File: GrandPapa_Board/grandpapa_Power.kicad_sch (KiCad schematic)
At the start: 33 parts, among them U1 LT1576IS8-5#TRPBF, U2 TPS61023DRLT, U5 FPF2124, U6 INA180

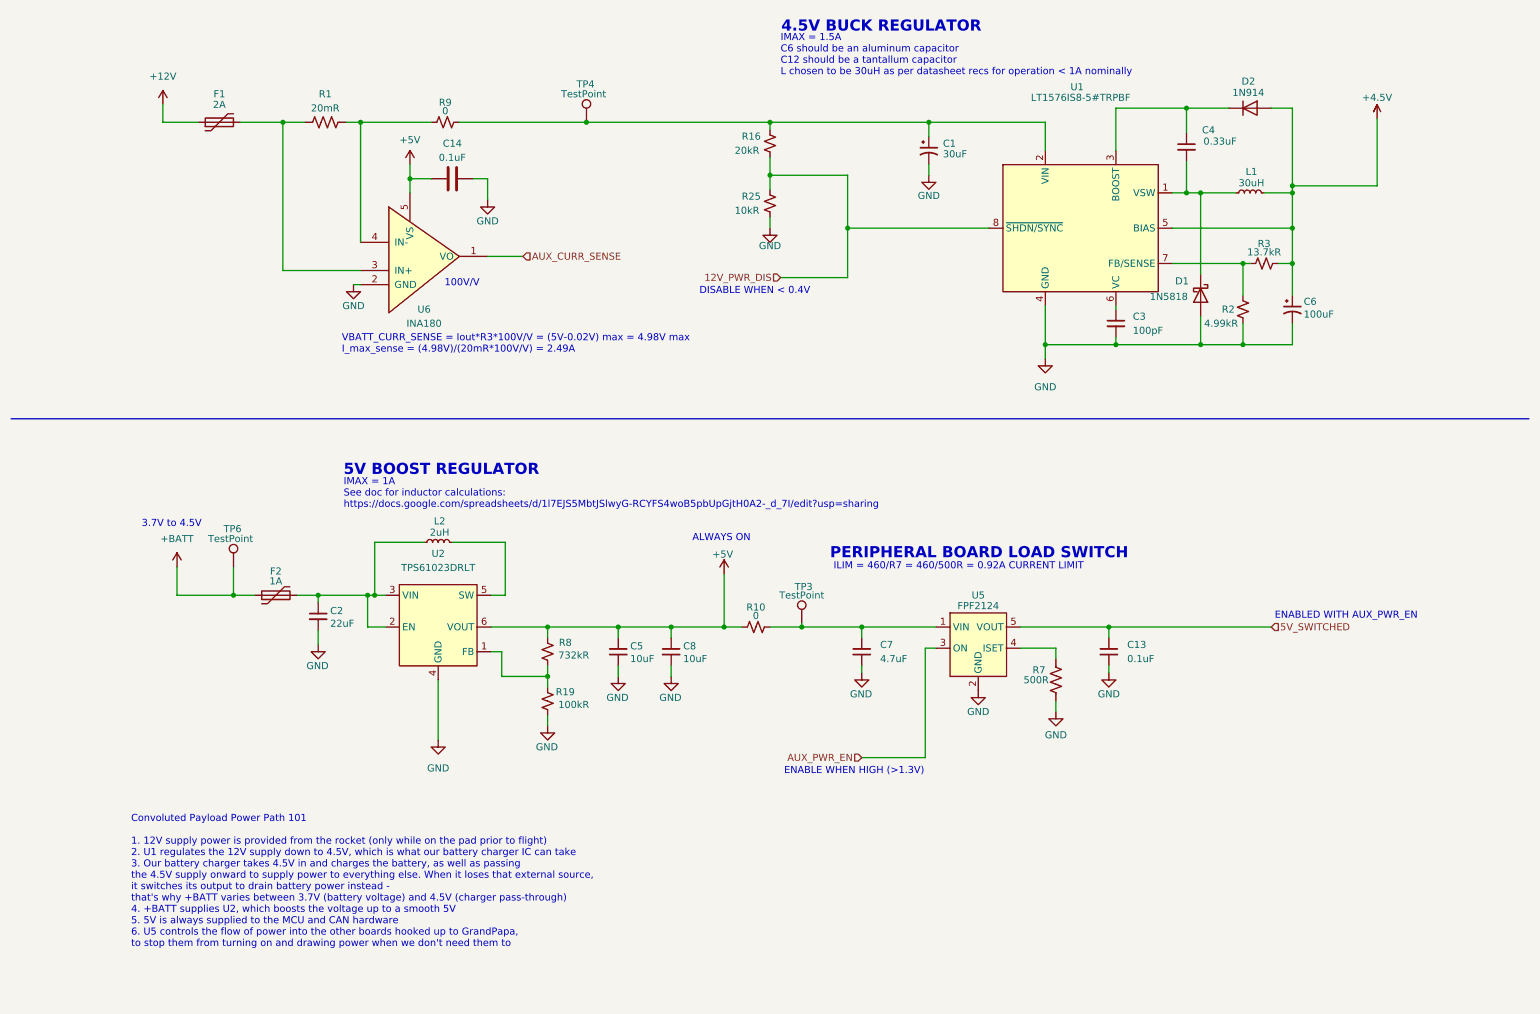
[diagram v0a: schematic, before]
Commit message: added new buck reg IC, external component values TBA
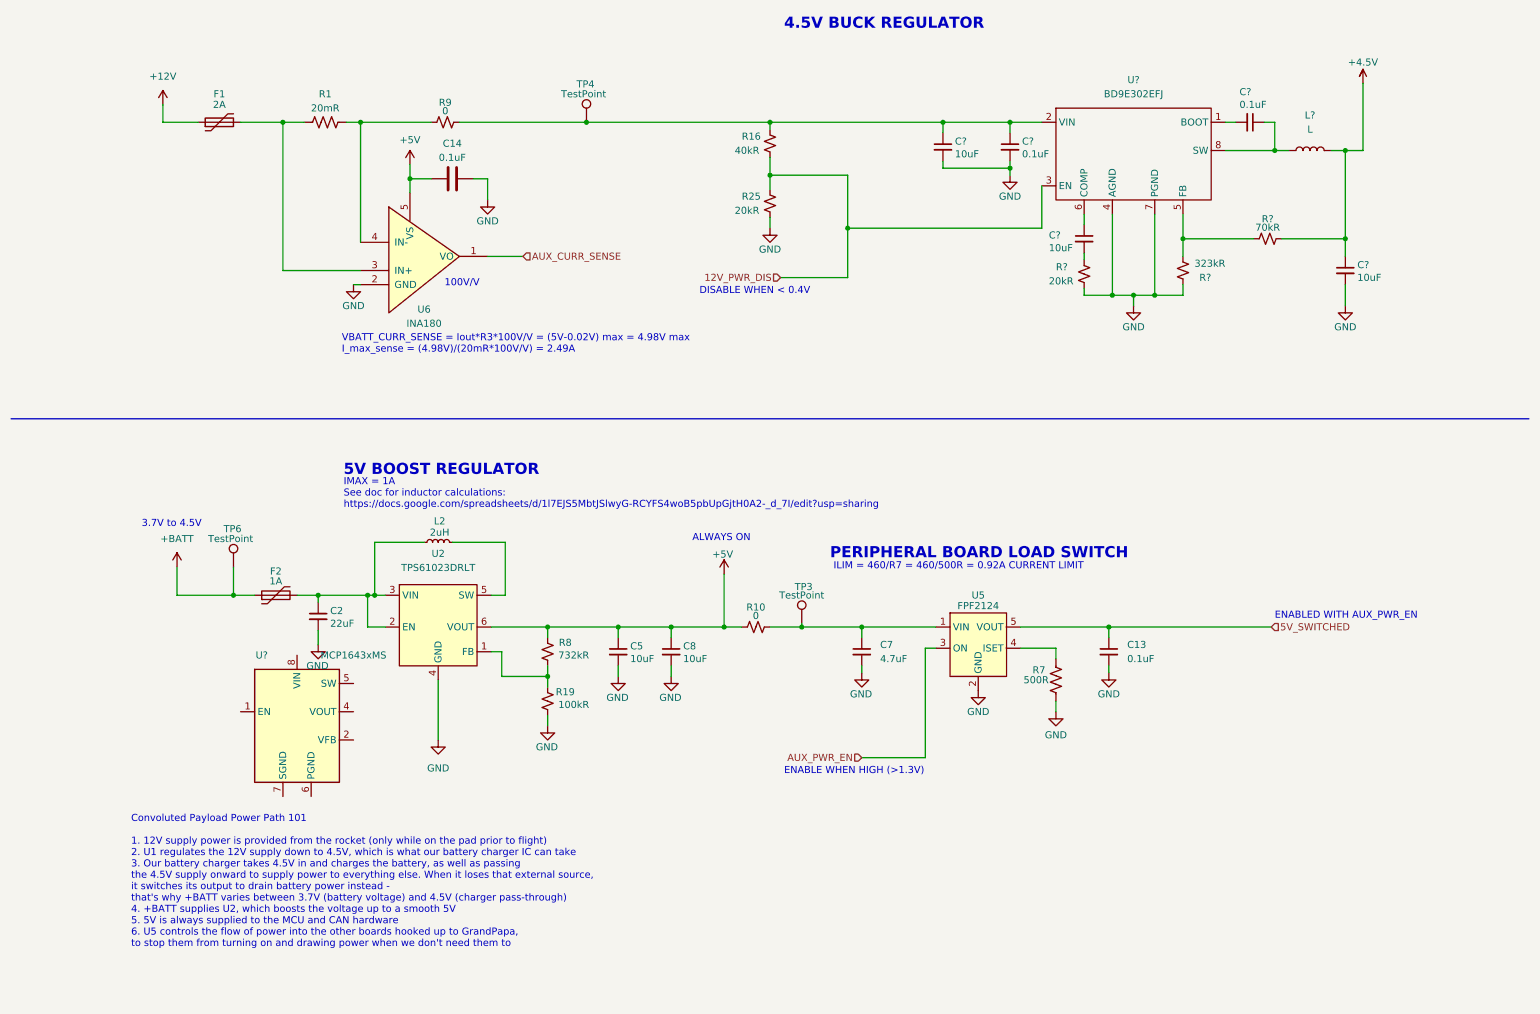
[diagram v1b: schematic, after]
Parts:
- removed C1: 30uF, symbol Device:C_Polarized_Small_US
- removed C3: 100pF, symbol Device:C_Small
- removed C4: 0.33uF, symbol Device:C_Small
- removed C6: 100uF, symbol Device:C_Polarized_Small_US
- removed D1: 1N5818, Diode_THT:D_DO-41_SOD81_P10.16mm_Horizontal, symbol Diode:1N5818
- removed D2: 1N914, Diode_THT:D_DO-35_SOD27_P7.62mm_Horizontal, symbol Diode:1N914
- removed L1: 30uH, symbol Device:L_Small
- removed R2: 4.99kR, symbol Device:R_Small_US
- removed R3: 13.7kR, symbol Device:R_Small_US
- removed U1: LT1576IS8-5#TRPBF, symbol grandpapa board:LT1576IS8-5#TRPBF
- added C? (x2): 0.1uF, symbol Device:C_Small
- added C? (x3): 10uF, symbol Device:C_Small
- added L?: L, symbol Device:L
- added R?: 70kR, symbol Device:R_Small_US
- added R?: 323kR, symbol Device:R_Small_US
- added R?: 20kR, symbol Device:R_Small_US
- added U?: MCP1643xMS, Package_SO:MSOP-8_3x3mm_P0.65mm, symbol Driver_LED:MCP1643xMS
- added U?: BD9E302EFJ, symbol grandpapa board:BD9E302EFJ
- R16: value 20kR -> 40kR
- R25: value 10kR -> 20kR
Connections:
- net +4.5V: now also C?.1, L?.2, R?.2
- net 12V_PWR_DIS: now also U?.3 (EN)
- net GND: now also C?.2, C?.2, C?.2, R?.1, R?.2, U?.4 (AGND), U?.7 (PGND)
- net at R16.2, R9.2, TP4.1: now also C?.1, C?.1, U?.2 (VIN)
- new net: R?.1, R?.1, U?.5 (FB)
- new net: C?.1, U?.6 (COMP)
- new net: C?.2, R?.2
- new net: C?.1, L?.1, U?.8 (SW)
- new net: C?.2, U?.1 (BOOT)
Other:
- note removed: "IMAX = 1.5A C6 should be an aluminum capacitor C12 should be a tantallum capacitor L chosen to be 30uH as per datasheet recs for operation < 1A nominally"

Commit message: more buck conv component sizing
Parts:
- removed U?: MCP1643xMS, Package_SO:MSOP-8_3x3mm_P0.65mm, symbol Driver_LED:MCP1643xMS
- C?: value 10uF -> ?
- R?: value 70kR -> 324kR
- R?: value 323kR -> 70kR

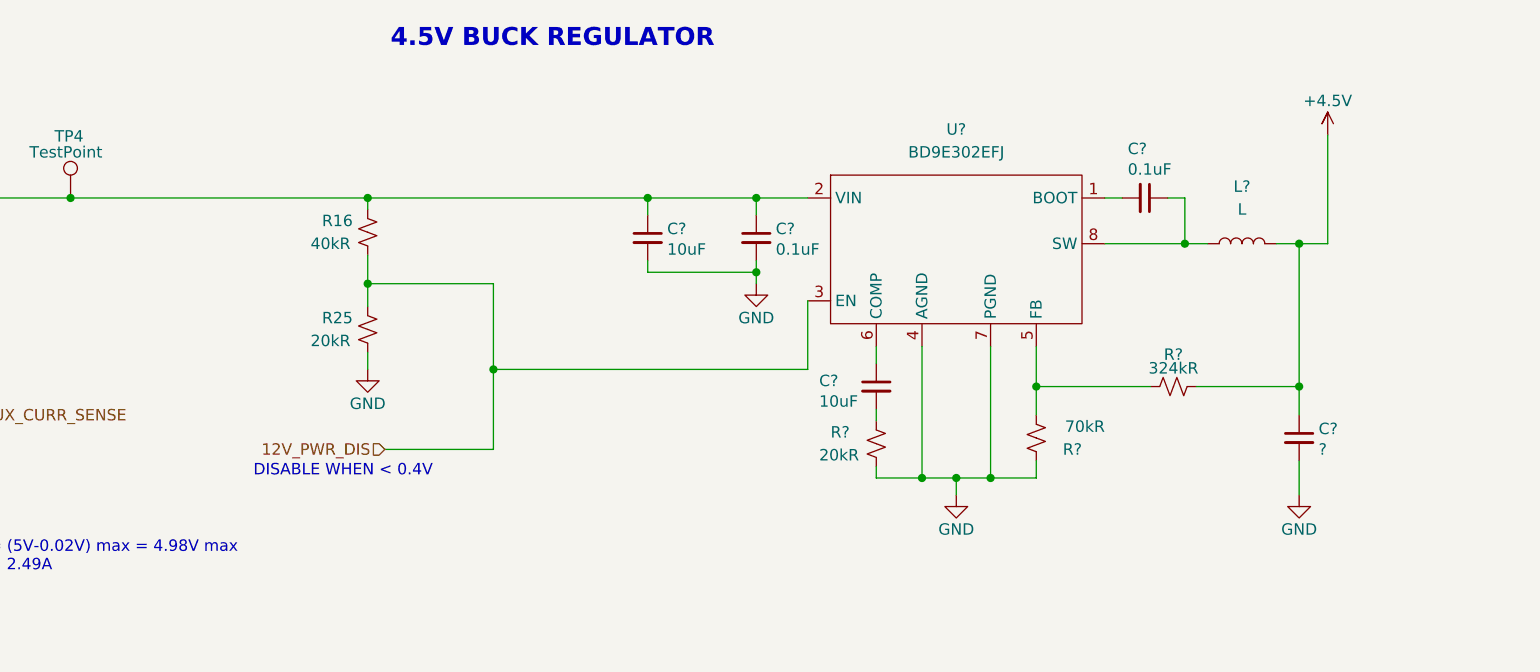
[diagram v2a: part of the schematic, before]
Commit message: component sizing for 4.5V buck complete
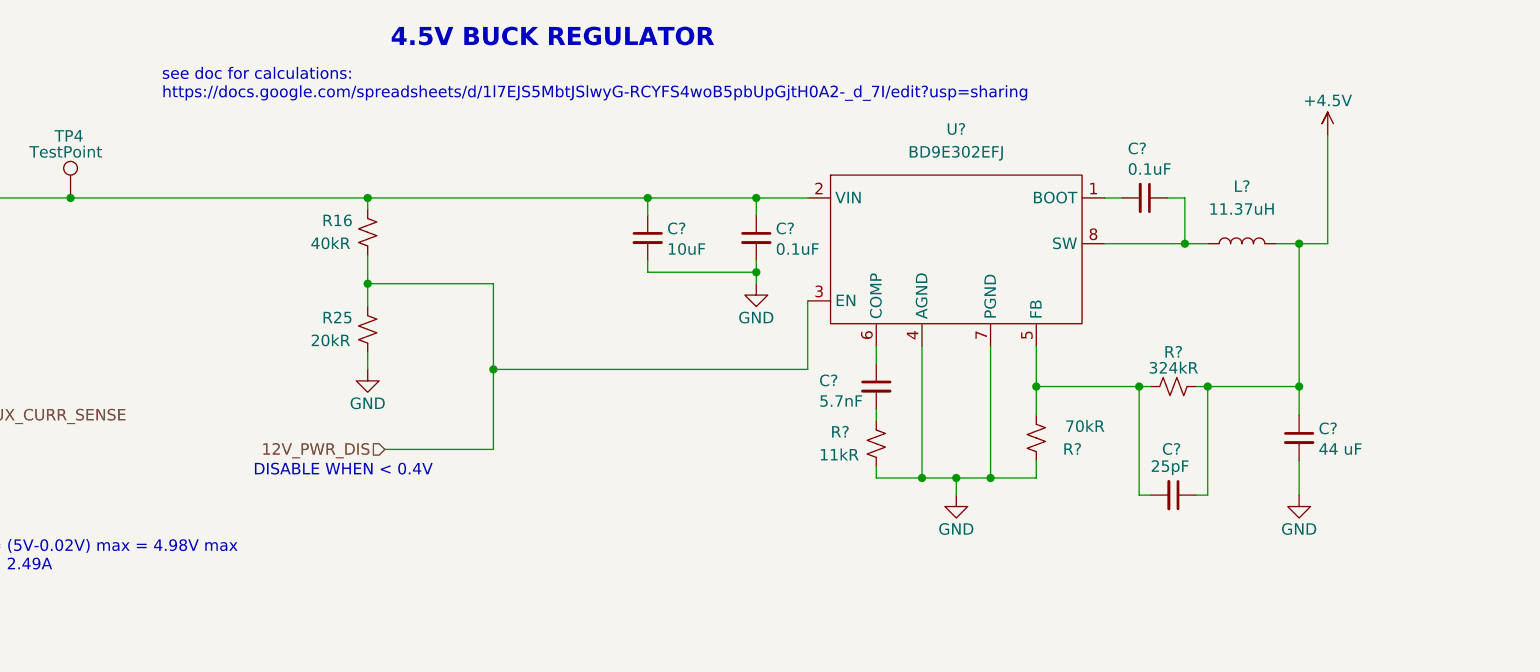
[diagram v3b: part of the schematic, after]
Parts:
- added C?: 25pF, symbol Device:C_Small
- C?: value 10uF -> 5.7nF
- C?: value ? -> 44 uF
- L?: value L -> 11.37uH
- R?: value 20kR -> 11kR
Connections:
- net +4.5V: now also C?.1
- net at R?.1, R?.1, U?.5 (FB): now also C?.2
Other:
- note added: "see doc for calculations: https://docs.google.com/spreadsheets/d/1l7EJS5MbtJSlwyG-RCYFS4woB5pbUpGjtH0A2-_d_7I/edit?usp=sharing"
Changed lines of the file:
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@@
   (junction (at 191.77 43.815) (diameter 0) (color 0 0 0 0)
   )
+  (junction (at 234.315 56.515) (diameter 0) (color 0 0 0 0)
+  )
   (junction (at 77.47 120.65) (diameter 0) (color 0 0 0 0)
   )
@@
   (junction (at 217.805 66.675) (diameter 0) (color 0 0 0 0)
   )
+  (junction (at 241.935 56.515) (diameter 0) (color 0 0 0 0)
+  )
   (junction (at 130.81 126.365) (diameter 0) (color 0 0 0 0)
   )
@@
     (stroke (width 0) (type default) (color 0 0 0 0))
   )
+  (wire (pts (xy 235.585 68.58) (xy 234.315 68.58))
+    (stroke (width 0) (type default) (color 0 0 0 0))
+  )
   (wire (pts (xy 150.495 63.5) (xy 162.56 63.5))
     (stroke (width 0) (type default) (color 0 0 0 0))
@@
     (stroke (width 0) (type default) (color 0 0 0 0))
   )
+  (wire (pts (xy 241.935 56.515) (xy 241.935 68.58))
+    (stroke (width 0) (type default) (color 0 0 0 0))
+  )
   (wire (pts (xy 176.53 149.86) (xy 176.53 130.175))
     (stroke (width 0) (type default) (color 0 0 0 0))
@@
     (stroke (width 0) (type default) (color 0 0 0 0))
   )
+  (wire (pts (xy 234.315 56.515) (xy 222.885 56.515))
+    (stroke (width 0) (type default) (color 0 0 0 0))
+  )
+  (wire (pts (xy 240.665 68.58) (xy 241.935 68.58))
+    (stroke (width 0) (type default) (color 0 0 0 0))
+  )
   (wire (pts (xy 209.55 134.62) (xy 209.55 133.35))
     (stroke (width 0) (type default) (color 0 0 0 0))
@@
     (stroke (width 0) (type default) (color 0 0 0 0))
   )
+  (wire (pts (xy 241.935 56.515) (xy 240.665 56.515))
+    (stroke (width 0) (type default) (color 0 0 0 0))
+  )
   (wire (pts (xy 255.27 28.575) (xy 255.27 40.64))
     (stroke (width 0) (type default) (color 0 0 0 0))
@@
     (stroke (width 0) (type default) (color 0 0 0 0))
   )
+  (wire (pts (xy 234.315 56.515) (xy 234.315 68.58))
+    (stroke (width 0) (type default) (color 0 0 0 0))
+  )
   (wire (pts (xy 230.505 35.56) (xy 232.41 35.56))
     (stroke (width 0) (type default) (color 0 0 0 0))
@@
     (stroke (width 0) (type default) (color 0 0 0 0))
   )
-  (wire (pts (xy 235.585 56.515) (xy 222.885 56.515))
+  (wire (pts (xy 235.585 56.515) (xy 234.315 56.515))
     (stroke (width 0) (type default) (color 0 0 0 0))
   )
@@
     (stroke (width 0) (type default) (color 0 0 0 0))
   )
+  (wire (pts (xy 241.935 56.515) (xy 252.095 56.515))
+    (stroke (width 0) (type default) (color 0 0 0 0))
+  )
   (wire (pts (xy 76.2 126.365) (xy 76.2 120.65))
     (stroke (width 0) (type default) (color 0 0 0 0))
@@
   )
   (wire (pts (xy 100.965 120.65) (xy 100.965 111.125))
-    (stroke (width 0) (type default) (color 0 0 0 0))
-  )
-  (wire (pts (xy 252.095 56.515) (xy 240.665 56.515))
     (stroke (width 0) (type default) (color 0 0 0 0))
   )
@@
   )
   (text "3.7V to 4.5V" (at 35.56 108.585 0)
+    (effects (font (size 1.27 1.27)) (justify left bottom))
+  )
+  (text "see doc for calculations:\nhttps://docs.google.com/spreadsheets/d/1l7EJS5MbtJSlwyG-RCYFS4woB5pbUpGjtH0A2-_d_7I/edit?usp=sharing"
+    (at 125.73 24.765 0)
     (effects (font (size 1.27 1.27)) (justify left bottom))
   )
@@
   (symbol (lib_id "Device:R_Small_US") (at 238.125 56.515 90) (unit 1)
     (in_bom yes) (on_board yes)
-    (property "Reference" "R?" (id 0) (at 238.125 52.959 90))
+    (property "Reference" "R?" (id 0) (at 238.125 52.705 90))
     (property "Value" "324kR" (id 1) (at 238.125 54.483 90))
     (property "Footprint" "" (id 2) (at 238.125 56.515 0)
@@
       (effects (font (size 1.27 1.27)) (justify left))
     )
-    (property "Value" "10uF" (id 1) (at 198.755 58.166 0)
+    (property "Value" "5.7nF" (id 1) (at 198.755 58.166 0)
       (effects (font (size 1.27 1.27)) (justify left))
     )
@@
     (in_bom yes) (on_board yes) (fields_autoplaced)
     (property "Reference" "L?" (id 0) (at 245.745 34.29 90))
-    (property "Value" "L" (id 1) (at 245.745 36.83 90))
+    (property "Value" "11.37uH" (id 1) (at 245.745 36.83 90))
     (property "Footprint" "" (id 2) (at 245.745 40.64 0)
       (effects (font (size 1.27 1.27)) hide)
@@
     )
     (property "Datasheet" "~" (id 3) (at 146.05 126.365 0)
+      (effects (font (size 1.27 1.27)) hide)
+    )
+    (pin "1")
+    (pin "2")
+  )
+  (symbol (lib_id "Device:C_Small") (at 238.125 68.58 270) (unit 1)
+    (in_bom yes) (on_board yes)
+    (property "Reference" "C?" (id 0) (at 236.855 63.5 90)
+      (effects (font (size 1.27 1.27)) (justify left))
+    )
+    (property "Value" "25pF" (id 1) (at 235.585 65.405 90)
+      (effects (font (size 1.27 1.27)) (justify left))
+    )
+    (property "Footprint" "" (id 2) (at 238.125 68.58 0)
+      (effects (font (size 1.27 1.27)) hide)
+    )
+    (property "Datasheet" "~" (id 3) (at 238.125 68.58 0)
       (effects (font (size 1.27 1.27)) hide)
     )
@@
       (effects (font (size 1.27 1.27)) (justify right))
     )
-    (property "Value" "20kR" (id 1) (at 198.755 64.135 0)
+    (property "Value" "11kR" (id 1) (at 198.755 64.135 0)
       (effects (font (size 1.27 1.27)) (justify right))
     )
@@
       (effects (font (size 1.27 1.27)) (justify left))
     )
-    (property "Value" "?" (id 1) (at 254.254 63.5 0)
-      (effects (font (size 1.27 1.27)) (justify left))
-    )
+    (property "Value" "44 uF" (id 1) (at 254.254 63.5 0)
+      (effects (font (size 1.27 1.27)) (justify left))
+    )
